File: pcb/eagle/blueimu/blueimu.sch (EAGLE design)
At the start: 26 parts, among them IC1 ICL7665CPA, IC2 ATMEGA328P, IC3 LP2950Z, J1 22-27-2021-02, Q1 IRL3803, Q2 7.3728MHz

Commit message: Removed unnecessary pull-up resistor from serial line. Added pull-down resistor for LED output.
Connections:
- net +3V3: no longer R10.1
- net GND: now also R10.2
- net PD2: now also R10.1
- net TXD: no longer R10.2
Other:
- note added: "Battery undervoltage signaling and over-discharge protection - LED goes off at 3.3 V - Battery disconnected from load at 3.0 V (typical value for LiPO)"
- note removed: "Note: For RX (TX on HC06) we use the internal pull-up of ATMEGA."
- moved on the sheet: R10
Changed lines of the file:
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@@
 <part name="GND12" library="supply1" deviceset="GND" device=""/>
 <part name="R10" library="rcl" deviceset="R-EU_" device="0207/7" value="10k"/>
-<part name="+3V6" library="supply1" deviceset="+3V3" device=""/>
+<part name="GND13" library="supply1" deviceset="GND" device=""/>
 </parts>
 <sheets>
 <sheet>
 <plain>
-<text x="93.98" y="-165.1" size="1.778" layer="91">Note: For RX (TX on HC06) we use the internal pull-up of ATMEGA.</text>
 <text x="-15.24" y="-165.1" size="1.778" layer="91">Note: GY521 has on-board pull-up resistors for SCL and SDA.</text>
+<text x="20.32" y="58.42" size="1.778" layer="91">Battery undervoltage signaling and over-discharge protection
+- LED goes off at 3.3 V
+- Battery disconnected from load at 3.0 V (typical value for LiPO)
+</text>
 </plain>
 <instances>
@@
 <instance part="GND4" gate="1" x="0" y="-106.68"/>
 <instance part="GND5" gate="1" x="-15.24" y="-106.68"/>
-<instance part="Q2" gate="G$1" x="-7.62" y="-76.2"/>
+<instance part="Q2" gate="G$1" x="-7.62" y="-76.2" smashed="yes">
+<attribute name="NAME" x="-5.08" y="-75.184" size="1.778" layer="95"/>
+<attribute name="VALUE" x="-13.462" y="-81.026" size="1.778" layer="96"/>
+</instance>
 <instance part="C5" gate="G$1" x="-15.24" y="-86.36"/>
 <instance part="C3" gate="G$1" x="0" y="-86.36"/>
@@
 <instance part="GND10" gate="1" x="-17.78" y="-152.4"/>
 <instance part="GND11" gate="1" x="55.88" y="-154.94"/>
-<instance part="GND12" gate="1" x="116.84" y="-157.48"/>
-<instance part="R10" gate="G$1" x="106.68" y="-137.16" rot="R270"/>
-<instance part="+3V6" gate="G$1" x="106.68" y="-127"/>
+<instance part="GND12" gate="1" x="116.84" y="-165.1"/>
+<instance part="R10" gate="G$1" x="106.68" y="-154.94" rot="R270"/>
+<instance part="GND13" gate="1" x="106.68" y="-165.1"/>
 </instances>
 <busses>
@@
 <pinref part="GND12" gate="1" pin="GND"/>
 <wire x1="124.46" y1="-152.4" x2="116.84" y2="-152.4" width="0.1524" layer="91"/>
-<wire x1="116.84" y1="-152.4" x2="116.84" y2="-154.94" width="0.1524" layer="91"/>
+<wire x1="116.84" y1="-152.4" x2="116.84" y2="-162.56" width="0.1524" layer="91"/>
+</segment>
+<segment>
+<pinref part="GND13" gate="1" pin="GND"/>
+<pinref part="R10" gate="G$1" pin="2"/>
+<wire x1="106.68" y1="-162.56" x2="106.68" y2="-160.02" width="0.1524" layer="91"/>
 </segment>
 </net>
@@
 <wire x1="-17.78" y1="-139.7" x2="-17.78" y2="-134.62" width="0.1524" layer="91"/>
 </segment>
-<segment>
-<pinref part="R10" gate="G$1" pin="1"/>
-<wire x1="106.68" y1="-132.08" x2="106.68" y2="-129.54" width="0.1524" layer="91"/>
-<pinref part="+3V6" gate="G$1" pin="+3V3"/>
-</segment>
 </net>
 <net name="N$15" class="0">
@@
 <segment>
 <pinref part="U$2" gate="G$1" pin="RX"/>
-<wire x1="124.46" y1="-142.24" x2="106.68" y2="-142.24" width="0.1524" layer="91"/>
-<label x="101.6" y="-142.24" size="1.778" layer="95" rot="R180" xref="yes"/>
-<wire x1="106.68" y1="-142.24" x2="101.6" y2="-142.24" width="0.1524" layer="91"/>
-<junction x="106.68" y="-142.24"/>
-<pinref part="R10" gate="G$1" pin="2"/>
+<wire x1="124.46" y1="-142.24" x2="121.92" y2="-142.24" width="0.1524" layer="91"/>
+<label x="121.92" y="-142.24" size="1.778" layer="95" rot="R180" xref="yes"/>
 </segment>
 </net>
@@
 <segment>
 <pinref part="U$2" gate="G$1" pin="LED"/>
-<wire x1="124.46" y1="-147.32" x2="121.92" y2="-147.32" width="0.1524" layer="91"/>
-<label x="121.92" y="-147.32" size="1.778" layer="95" rot="R180" xref="yes"/>
+<wire x1="124.46" y1="-147.32" x2="106.68" y2="-147.32" width="0.1524" layer="91"/>
+<label x="101.6" y="-147.32" size="1.778" layer="95" rot="R180" xref="yes"/>
+<pinref part="R10" gate="G$1" pin="1"/>
+<wire x1="106.68" y1="-147.32" x2="101.6" y2="-147.32" width="0.1524" layer="91"/>
+<wire x1="106.68" y1="-149.86" x2="106.68" y2="-147.32" width="0.1524" layer="91"/>
+<junction x="106.68" y="-147.32"/>
 </segment>
 </net>
@@
 </schematic>
 </drawing>
+<compatibility>
+<note version="6.3" minversion="6.2.2" severity="warning">
+Since Version 6.2.2 text objects can contain more than one line,
+which will not be processed correctly with this version.
+</note>
+</compatibility>
 </eagle>

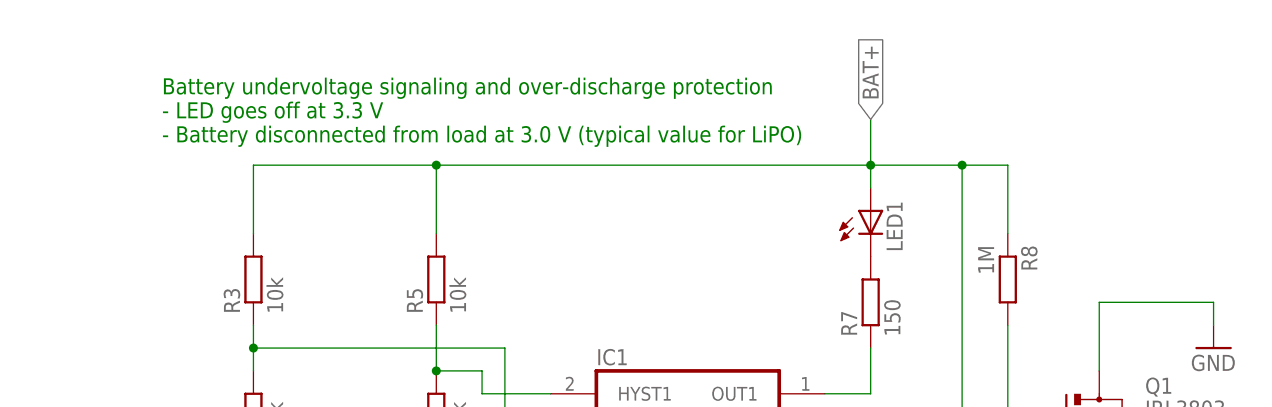
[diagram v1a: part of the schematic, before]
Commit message: Cosmetic changes to schematics and board layout
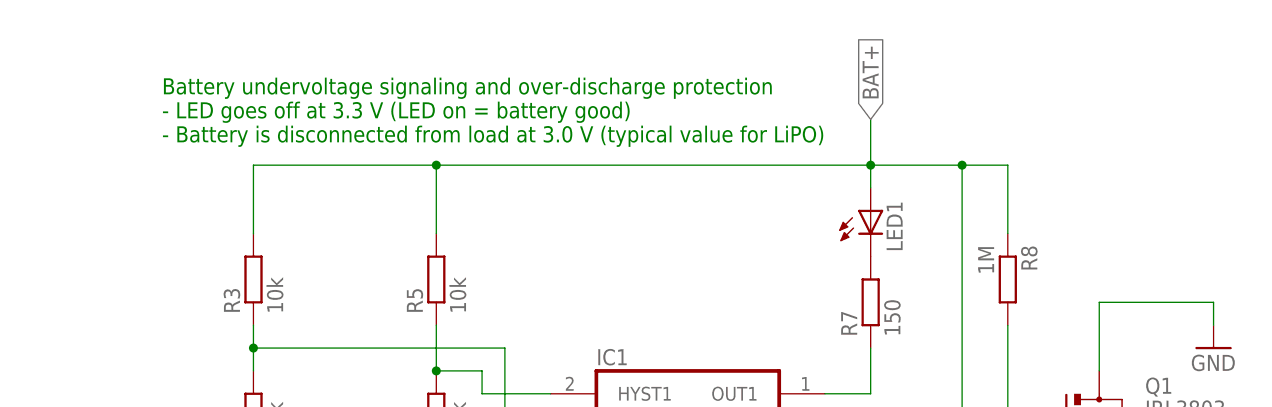
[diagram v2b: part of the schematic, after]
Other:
- note added: "Battery undervoltage signaling and over-discharge protection - LED goes off at 3.3 V (LED on = battery good) - Battery is disconnected from load at 3.0 V (typical value for LiPO)"
- note removed: "Battery undervoltage signaling and over-discharge protection - LED goes off at 3.3 V - Battery disconnected from load at 3.0 V (typical value for LiPO)"
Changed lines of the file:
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@@
 <text x="-15.24" y="-165.1" size="1.778" layer="91">Note: GY521 has on-board pull-up resistors for SCL and SDA.</text>
 <text x="20.32" y="58.42" size="1.778" layer="91">Battery undervoltage signaling and over-discharge protection
-- LED goes off at 3.3 V
-- Battery disconnected from load at 3.0 V (typical value for LiPO)
+- LED goes off at 3.3 V (LED on = battery good)
+- Battery is disconnected from load at 3.0 V (typical value for LiPO)
 </text>
 </plain>

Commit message: Added capacitor. Added Gerber files.
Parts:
- added C7: 100nF, rcl:C-EU050-024X044
- R8: value 1M -> 470k
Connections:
- net BAT-: now also C7.2
- net N$9: now also C7.1
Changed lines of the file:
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@@
 <part name="R7" library="rcl" deviceset="R-EU_" device="0207/7" value="150"/>
 <part name="GND1" library="supply1" deviceset="GND" device=""/>
-<part name="R8" library="rcl" deviceset="R-EU_" device="0207/7" value="1M"/>
+<part name="R8" library="rcl" deviceset="R-EU_" device="0207/7" value="470k"/>
 <part name="J1" library="con-molex" deviceset="22-?-02" device="27-2021"/>
 <part name="IC2" library="atmel" deviceset="MEGA8-P" device="" value="ATMEGA328P"/>
@@
 <part name="R10" library="rcl" deviceset="R-EU_" device="0207/7" value="10k"/>
 <part name="GND13" library="supply1" deviceset="GND" device=""/>
+<part name="C7" library="rcl" deviceset="C-EU" device="050-024X044" value="100nF"/>
 </parts>
 <sheets>
@@
 <instance part="R10" gate="G$1" x="106.68" y="-154.94" rot="R270"/>
 <instance part="GND13" gate="1" x="106.68" y="-165.1"/>
+<instance part="C7" gate="G$1" x="114.3" y="15.24"/>
 </instances>
 <busses>
@@
 <pinref part="Q1" gate="G$1" pin="S"/>
 <wire x1="124.46" y1="22.86" x2="124.46" y2="2.54" width="0.1524" layer="91"/>
-<wire x1="124.46" y1="2.54" x2="99.06" y2="2.54" width="0.1524" layer="91"/>
+<wire x1="124.46" y1="2.54" x2="114.3" y2="2.54" width="0.1524" layer="91"/>
 <pinref part="R4" gate="G$1" pin="1"/>
+<wire x1="114.3" y1="2.54" x2="99.06" y2="2.54" width="0.1524" layer="91"/>
 <wire x1="30.48" y1="5.08" x2="30.48" y2="2.54" width="0.1524" layer="91"/>
 <wire x1="30.48" y1="2.54" x2="50.8" y2="2.54" width="0.1524" layer="91"/>
 <junction x="50.8" y="2.54"/>
+<pinref part="C7" gate="G$1" pin="2"/>
+<wire x1="114.3" y1="10.16" x2="114.3" y2="2.54" width="0.1524" layer="91"/>
+<junction x="114.3" y="2.54"/>
 </segment>
 <segment>
@@
 <wire x1="114.3" y1="38.1" x2="114.3" y2="25.4" width="0.1524" layer="91"/>
 <junction x="114.3" y="25.4"/>
-</segment>
-</net>
+<pinref part="C7" gate="G$1" pin="1"/>
+<wire x1="114.3" y1="17.78" x2="114.3" y2="25.4" width="0.1524" layer="91"/>
+</segment>
+</net>

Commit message: Extended Readme.
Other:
- note added: "BlueIMU V1.0 Copyright 2016 Frank Dürr Licensed under the CERN Open Hardware Licence 2.0"
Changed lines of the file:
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@@
 - Battery is disconnected from load at 3.0 V (typical value for LiPO)
 </text>
+<text x="-17.78" y="81.28" size="1.778" layer="91">BlueIMU V1.0
+Copyright 2016 Frank Dürr
+Licensed under the CERN Open Hardware Licence 2.0</text>
 </plain>
 <instances>
